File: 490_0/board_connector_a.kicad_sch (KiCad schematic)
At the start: 28 parts, among them J3 DF40C-100DS-0.4V_51_, J4 DF40C-100DS-0.4V_51_, Q2 NMOS, SW1 SW_DPST_x2

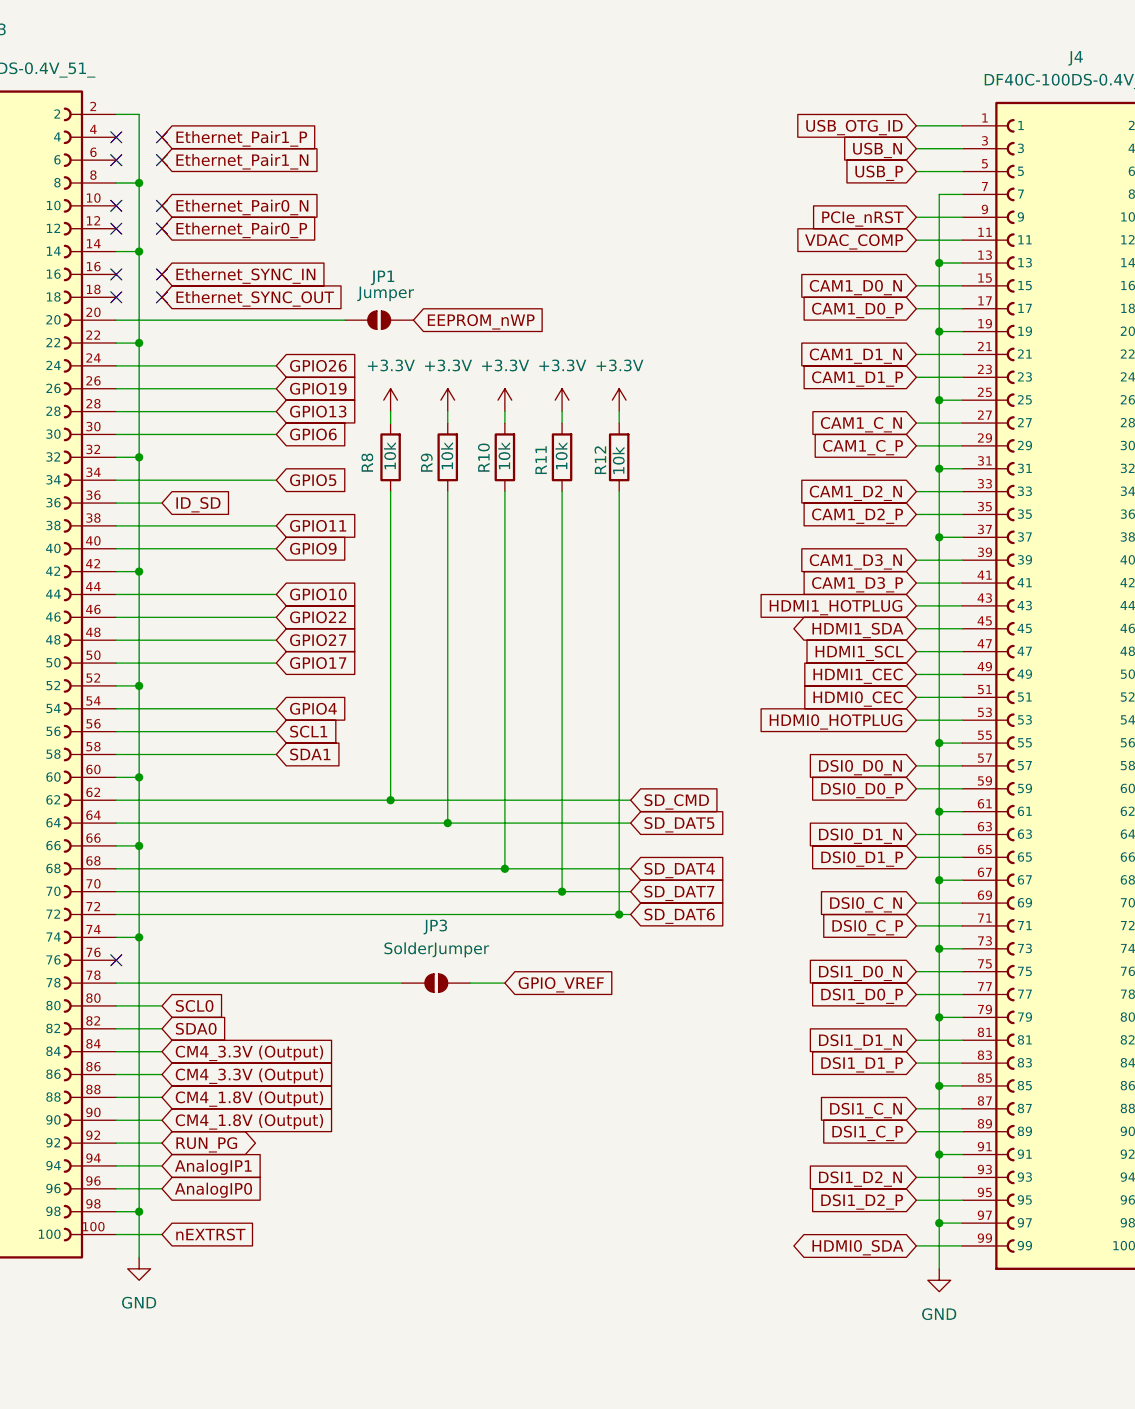
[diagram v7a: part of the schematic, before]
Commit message: USB2.0
Added USB2.0 circuit
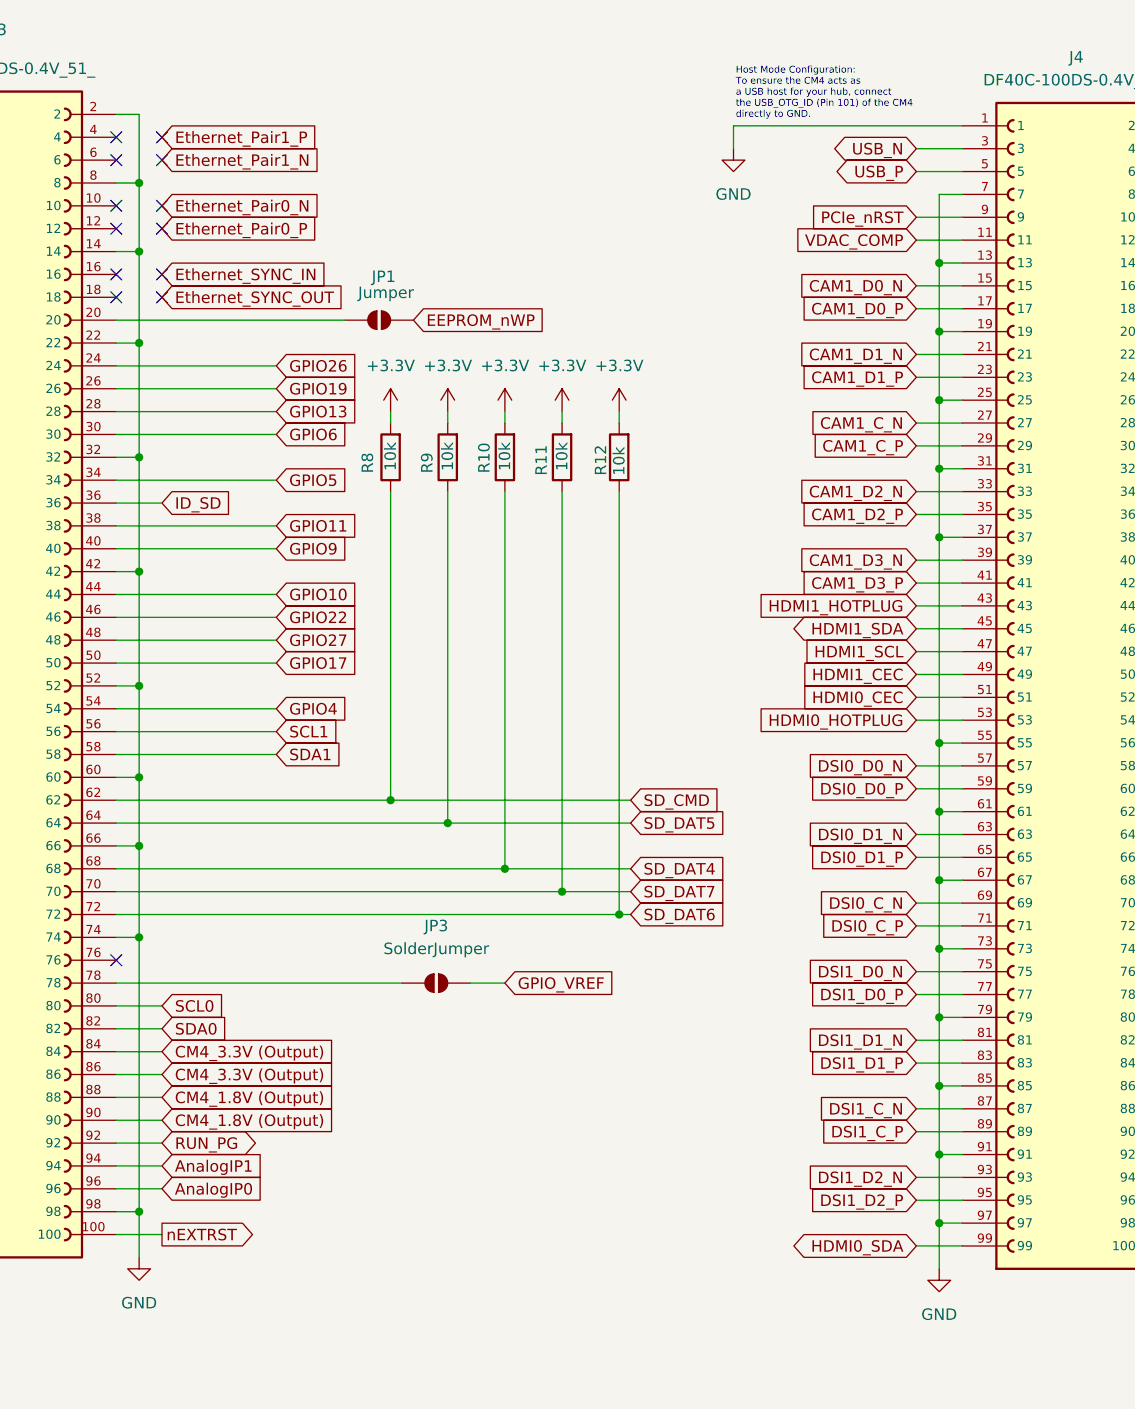
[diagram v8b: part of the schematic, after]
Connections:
- net USB_OTG_ID is gone; now on net GND: J4.1
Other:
- note added: "Host Mode Configuration: To ensure the CM4 acts as a USB host for your hub, connect the USB_OTG_ID (Pin 101) of the CM4 directly to GND."
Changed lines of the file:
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@@
 	(generator_version "9.0")
 	(paper "USLetter")
+	(text "Host Mode Configuration: \nTo ensure the CM4 acts as \na USB host for your hub, connect \nthe USB_OTG_ID (Pin 101) of the CM4 \ndirectly to GND."
+		(exclude_from_sim no)
+		(at 193.294 24.384 0)
+		(effects
+			(font
+				(size 0.762 0.762)
+			)
+			(justify left)
+		)
+	)
 	(text "nRPIBOOT"
 		(exclude_from_sim no)
@@
 	(wire
 		(pts
+			(xy 193.04 30.48) (xy 193.04 27.94)
+		)
+		(stroke
+			(width 0)
+			(type default)
+		)
+	)
+	(wire
+		(pts
 			(xy 127 77.47) (xy 127 90.17)
 		)
@@
 	(wire
 		(pts
+			(xy 193.04 27.94) (xy 218.44 27.94)
+		)
+		(stroke
+			(width 0)
+			(type default)
+		)
+	)
+	(wire
+		(pts
 			(xy 215.9 73.66) (xy 218.44 73.66)
 		)
@@
 	(wire
 		(pts
-			(xy 213.36 27.94) (xy 218.44 27.94)
-		)
-		(stroke
-			(width 0)
-			(type default)
-		)
-	)
-	(wire
-		(pts
 			(xy 213.36 106.68) (xy 218.44 106.68)
 		)
@@
 	)
 	(global_label "USB_P"
-		(shape input)
+		(shape bidirectional)
 		(at 213.36 33.02 180)
 		(effects
@@
 	)
 	(global_label "nEXTRST"
-		(shape input)
+		(shape output)
 		(at 129.54 151.13 0)
 		(effects
@@
 		)
 	)
-	(global_label "USB_OTG_ID"
-		(shape input)
-		(at 213.36 27.94 180)
-		(effects
-			(font
-				(size 1.27 1.27)
-			)
-			(justify right)
-		)
-		(property "Intersheetrefs" "${INTERSHEET_REFS}"
-			(at 213.36 27.94 0)
-			(effects
-				(font
-					(size 1.27 1.27)
-				)
-				(hide yes)
-			)
-		)
-	)
 	(global_label "HDMI1_SDA"
 		(shape bidirectional)
@@
 	)
 	(global_label "USB_N"
-		(shape input)
+		(shape bidirectional)
 		(at 213.36 30.48 180)
 		(effects
@@
 					(unit 1)
 				)
+			)
+		)
+	)
+	(symbol
+		(lib_id "power:GND")
+		(at 193.04 30.48 0)
+		(unit 1)
+		(exclude_from_sim no)
+		(in_bom yes)
+		(on_board yes)
+		(dnp no)
+		(fields_autoplaced yes)
+		(property "Reference" "#PWR09"
+			(at 193.04 36.83 0)
+			(effects
+				(font
+					(size 1.27 1.27)
+				)
+				(hide yes)
+			)
+		)
+		(property "Value" "GND"
+			(at 193.04 35.56 0)
+			(effects
+				(font
+					(size 1.27 1.27)
+				)
+			)
+		)
+		(property "Footprint" ""
+			(at 193.04 30.48 0)
+			(effects
+				(font
+					(size 1.27 1.27)
+				)
+				(hide yes)
+			)
+		)
+		(property "Datasheet" ""
+			(at 193.04 30.48 0)
+			(effects
+				(font
+					(size 1.27 1.27)
+				)
+				(hide yes)
+			)
+		)
+		(property "Description" "Power symbol creates a global label with name \"GND\" , ground"
+			(at 193.04 30.48 0)
+			(effects
+				(font
+					(size 1.27 1.27)
+				)
+				(hide yes)
+			)
+		)
+		(pin "1"
+		)
+		(instances
+			(project "490_0"
+				(path "/365a82ed-827d-43e1-aa2f-b98221c4179c/57a94eab-3ef7-4459-81a7-ccf0f968a3f9"
+					(reference "#PWR09")
+					(unit 1)
+				)
